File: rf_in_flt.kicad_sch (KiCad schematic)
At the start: 1 part, among them J2 Conn_Coaxial

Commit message: Add files via upload
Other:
- note added: "No filters here yet"
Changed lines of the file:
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@@
     (stroke (width 0) (type default))
+  )
+  (text "No filters here yet" (at 195.58 134.62 0)
+    (effects (font (size 1.27 1.27)) (justify left bottom))
   )
   (hierarchical_label "RF_OUT" (shape output) (at 194.31 138.43 180) (fields_autoplaced)
@@
         )
         (path "/4c42207c-9e6b-42da-ad38-da126b892014/548d001d-7c84-4d2c-957b-c97be3023400"
-          (reference "J5") (unit 1)
+          (reference "J6") (unit 1)
         )
       )
@@
         )
         (path "/4c42207c-9e6b-42da-ad38-da126b892014/548d001d-7c84-4d2c-957b-c97be3023400"
-          (reference "#PWR0109") (unit 1)
+          (reference "#PWR0110") (unit 1)
         )
       )

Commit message: PN update
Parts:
- J2: PN (none) -> -
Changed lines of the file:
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@@
+      (effects (font (size 1.27 1.27)) hide)
+    )
+    (property "PN" "-" (at 215.9 138.43 0)
       (effects (font (size 1.27 1.27)) hide)
     )

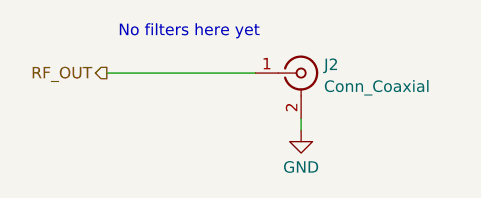
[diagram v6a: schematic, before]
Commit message: TP updates, temp sensor added
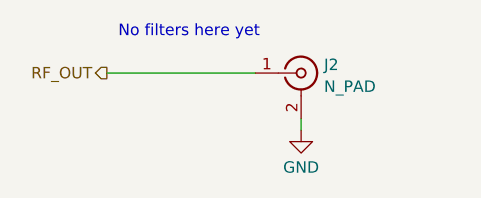
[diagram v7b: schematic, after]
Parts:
- J2: value Conn_Coaxial -> N_PAD
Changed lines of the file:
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@@
       (effects (font (size 1.27 1.27)) (justify left))
     )
-    (property "Value" "Conn_Coaxial" (at 218.4401 139.9353 0)
+    (property "Value" "N_PAD" (at 218.4401 139.9353 0)
       (effects (font (size 1.27 1.27)) (justify left))
     )
@@
         )
         (path "/4c42207c-9e6b-42da-ad38-da126b892014/548d001d-7c84-4d2c-957b-c97be3023400"
-          (reference "J6") (unit 1)
+          (reference "J7") (unit 1)
         )
       )
@@
         )
         (path "/4c42207c-9e6b-42da-ad38-da126b892014/548d001d-7c84-4d2c-957b-c97be3023400"
-          (reference "#PWR0115") (unit 1)
+          (reference "#PWR0120") (unit 1)
         )
       )
